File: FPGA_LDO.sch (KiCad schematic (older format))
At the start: 65 parts, among them J901 JTAG, Q901 2N3904, SW901 RESET, U901 LM317_3PinPackage, U902 AMS1117-3.3, U903 W25Q128JVS, U904 XC6SLX9-TQG144

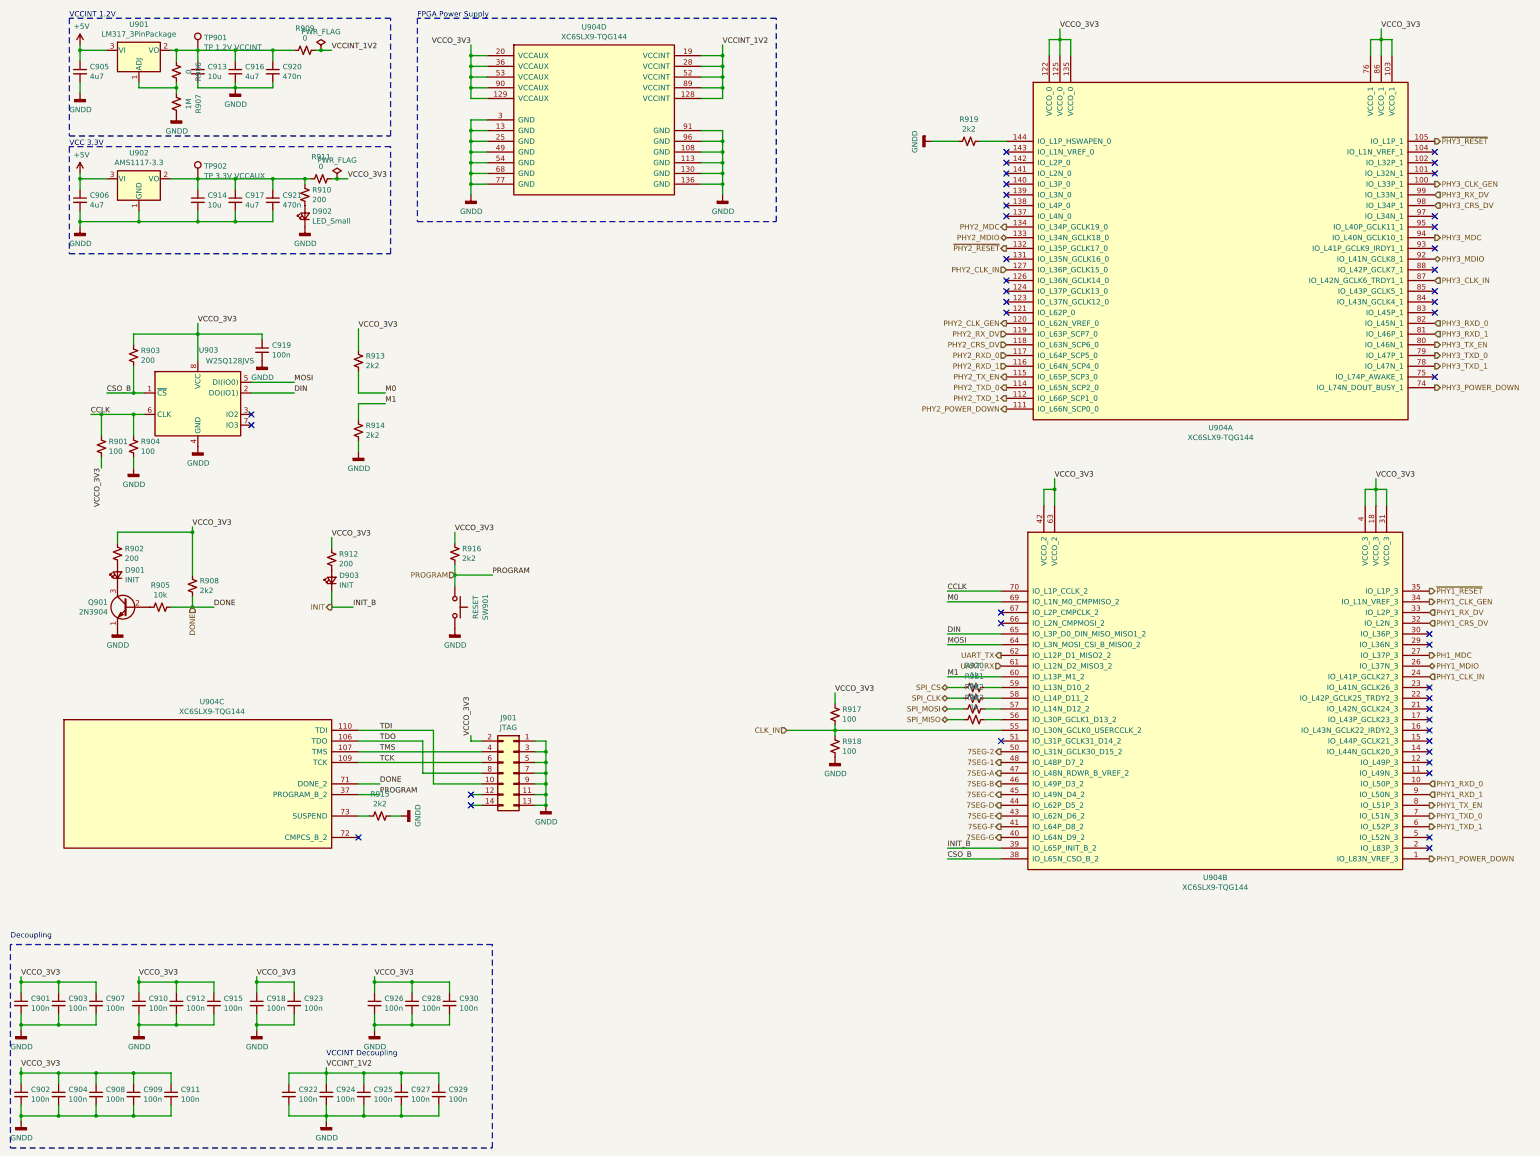
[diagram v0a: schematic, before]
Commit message: PCB layout 90% finished
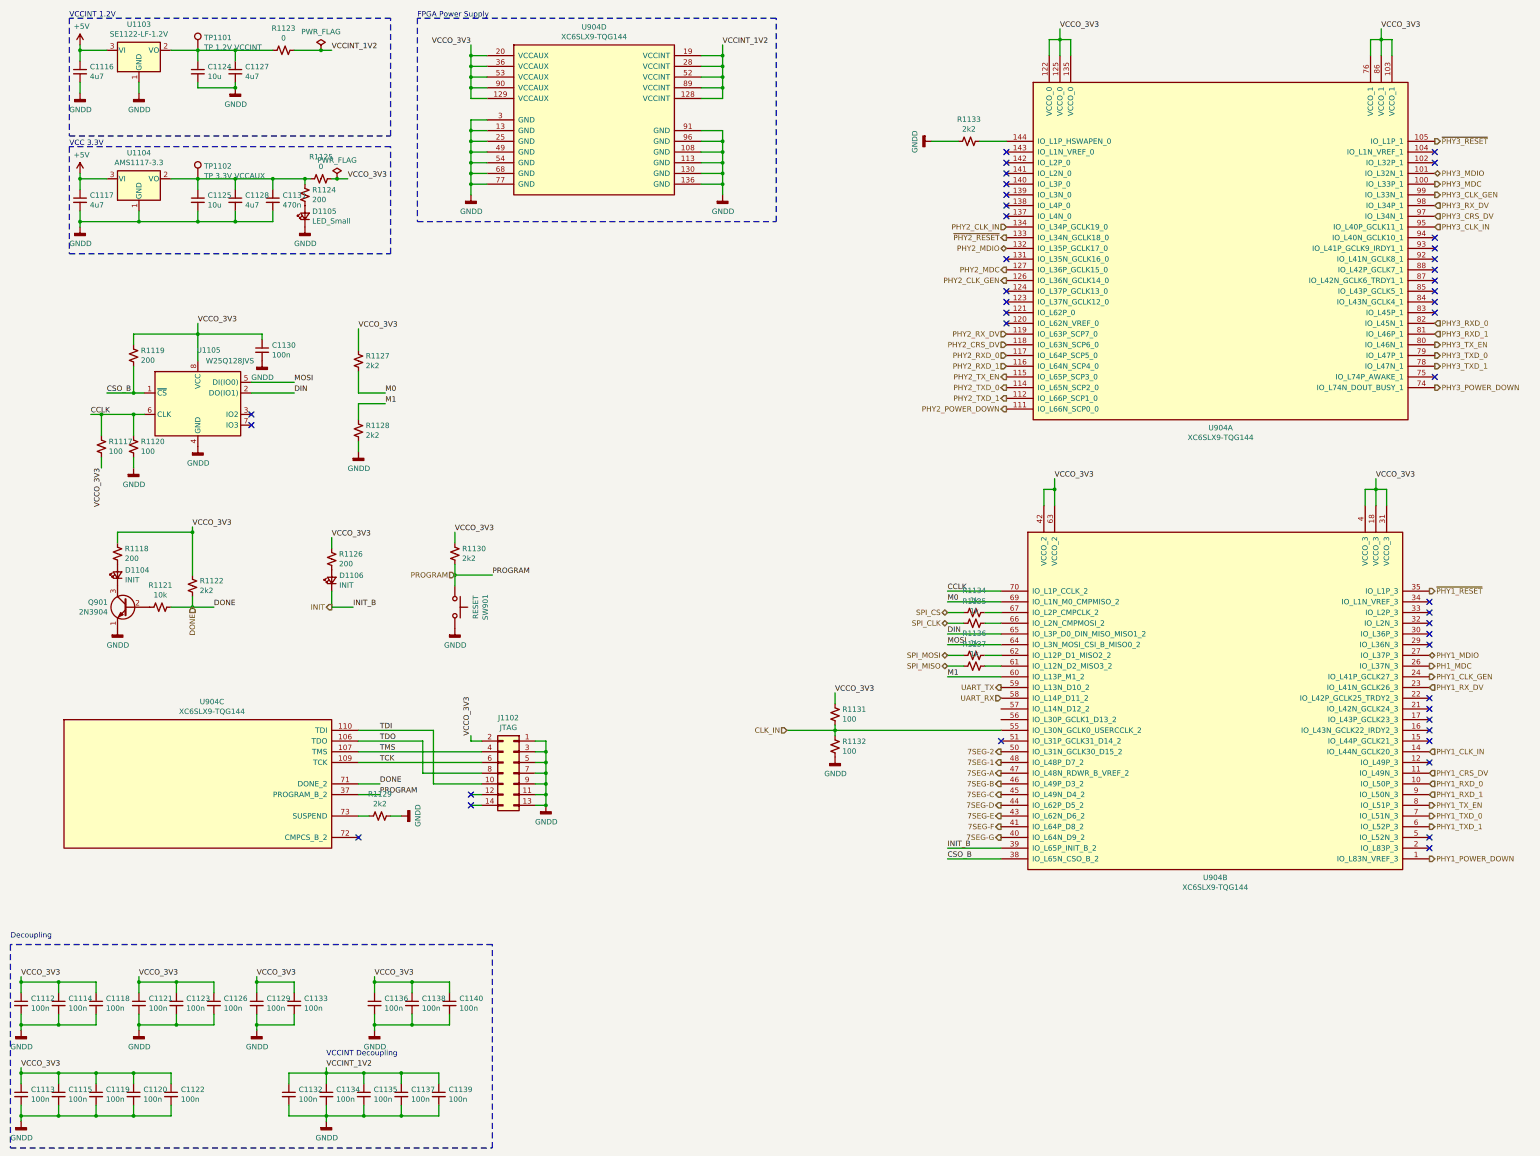
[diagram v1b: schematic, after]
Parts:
- removed C920: 470n, Capacitor_SMD:C_0402_1005Metric, symbol Device:C_Small
- removed R906: 0, Resistor_SMD:R_0402_1005Metric, symbol Device:R_Small_US
- removed R907: 1M, Resistor_SMD:R_0402_1005Metric, symbol Device:R_Small_US
- removed U901: LM317_3PinPackage, Package_TO_SOT_SMD:TO-252-2, symbol Regulator_Linear:LM317_3PinPackage
- added U1103: SE1122-LF-1.2V, Package_TO_SOT_SMD:SOT-223-3_TabPin2, symbol Regulator_Linear:LD1117S12TR_SOT223
- TP1101: renamed from TP901; footprint TestPoint:TestPoint_Keystone_5015_Micro-Minature -> TestPoint:TestPoint_Pad_D1.0mm
- TP1102: renamed from TP902; footprint TestPoint:TestPoint_Keystone_5015_Micro-Minature -> TestPoint:TestPoint_Pad_D1.0mm
- renumbered C901 to C1112, C902 to C1113, C903 to C1114, C904 to C1115, C905 to C1116, C906 to C1117, C907 to C1118, C908 to C1119, C909 to C1120, C910 to C1121, C911 to C1122, C912 to C1123, C913 to C1124, C914 to C1125, C915 to C1126, C916 to C1127, C917 to C1128, C918 to C1129, C919 to C1130, C921 to C1131, C922 to C1132, C923 to C1133, C924 to C1134, C925 to C1135, C926 to C1136, C927 to C1137, C928 to C1138, C929 to C1139, C930 to C1140, D901 to D1104, D902 to D1105, D903 to D1106, J901 to J1102, R901 to R1117, R902 to R1118, R903 to R1119, R904 to R1120, R905 to R1121, R908 to R1122, R909 to R1123, R910 to R1124, R911 to R1125, R912 to R1126, R913 to R1127, R914 to R1128, R915 to R1129, R916 to R1130, R917 to R1131, R918 to R1132, R919 to R1133, R920 to R1134, R921 to R1135, R922 to R1136, R923 to R1137, U902 to U1104, U903 to U1105
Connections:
- net +5V: now also U1103.3 (VI)
- net GNDD: now also U1103.1 (GND)
- net PH1_MDC: now also U904.26 (IO_L37N_3); no longer U904.27 (IO_L37P_3)
- net PHY1_CLK_GEN: now also U904.24 (IO_L41P_GCLK27_3); no longer U904.34 (IO_L1N_VREF_3)
- net PHY1_CLK_IN: now also U904.14 (IO_L44N_GCLK20_3); no longer U904.24 (IO_L41P_GCLK27_3)
- net PHY1_CRS_DV: now also U904.11 (IO_L49N_3); no longer U904.32 (IO_L2N_3)
- net PHY1_MDIO: now also U904.27 (IO_L37P_3); no longer U904.26 (IO_L37N_3)
- net PHY1_RX_DV: now also U904.23 (IO_L41N_GCLK26_3); no longer U904.33 (IO_L2P_3)
- net PHY2_CLK_GEN: now also U904.126 (IO_L36N_GCLK14_0); no longer U904.120 (IO_L62N_VREF_0)
- net PHY2_CLK_IN: now also U904.134 (IO_L34P_GCLK19_0); no longer U904.127 (IO_L36P_GCLK15_0)
- net PHY2_MDC: now also U904.127 (IO_L36P_GCLK15_0); no longer U904.134 (IO_L34P_GCLK19_0)
- net PHY2_MDIO: now also U904.132 (IO_L35P_GCLK17_0); no longer U904.133 (IO_L34N_GCLK18_0)
- net PHY3_CLK_GEN: now also U904.99 (IO_L33N_1); no longer U904.100 (IO_L33P_1)
- net PHY3_CLK_IN: now also U904.95 (IO_L40P_GCLK11_1); no longer U904.87 (IO_L42N_GCLK6_TRDY1_1)
- net PHY3_CRS_DV: now also U904.97 (IO_L34N_1); no longer U904.98 (IO_L34P_1)
- net PHY3_MDC: now also U904.100 (IO_L33P_1); no longer U904.94 (IO_L40N_GCLK10_1)
- net PHY3_MDIO: now also U904.101 (IO_L32N_1); no longer U904.92 (IO_L41N_GCLK8_1)
- net PHY3_RX_DV: now also U904.98 (IO_L34P_1); no longer U904.99 (IO_L33N_1)
- net UART_RX: now also U904.58 (IO_L14P_D11_2); no longer U904.61 (IO_L12N_D2_MISO3_2)
- net UART_TX: now also U904.59 (IO_L13N_D10_2); no longer U904.62 (IO_L12P_D1_MISO2_2)
- net ~PHY2_RESET: now also U904.133 (IO_L34N_GCLK18_0); no longer U904.132 (IO_L35P_GCLK17_0)
- net at C1124.1, C1127.1, R1123.2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: now also U1103.2 (VO)
- net at U904.56 (IO_L30P_GCLK1_D13_2): no longer R1137.1
- net at U904.57 (IO_L14N_D12_2): no longer R1136.1
- net at R1135.1: now also U904.66 (IO_L2N_CMPMOSI_2); no longer U904.58 (IO_L14P_D11_2)
- net at R1134.1: now also U904.67 (IO_L2P_CMPCLK_2); no longer U904.59 (IO_L13N_D10_2)
- new net: R1137.1, U904.61 (IO_L12N_D2_MISO3_2)
- new net: R1136.1, U904.62 (IO_L12P_D1_MISO2_2)
- no-connect marks 44 -> 42
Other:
- moved on the sheet: R1123, R1134, R1135, R1136, R1137
